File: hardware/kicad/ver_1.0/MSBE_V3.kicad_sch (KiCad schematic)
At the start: 179 parts, among them J1 USB_C_Receptacle_USB2.0_16P, J10 Low-V, J2 USB_C_Receptacle_USB2.0_16P, J3 Touch Pads, J4 Touch Pads, J5 UART, J6 Prog, J7 UART, J8 Prog, J9 High-V, U1 NPM1100-CAAA-R7, U10 MAX98357AEWL_T, U2 NPM1100-CAAA-R7, U3 NRF5340-CLAA-R, U4 NRF5340-CLAA-R, U5 BMA400, U6 BMA400, U7 MPR121QR2, U8 MPR121QR2, U9 MAX98357AEWL_T, Y1 32MHz, Y2 Crystal, Y3 32.768kHz, Y4 32.768kHz, Y5 32MHz

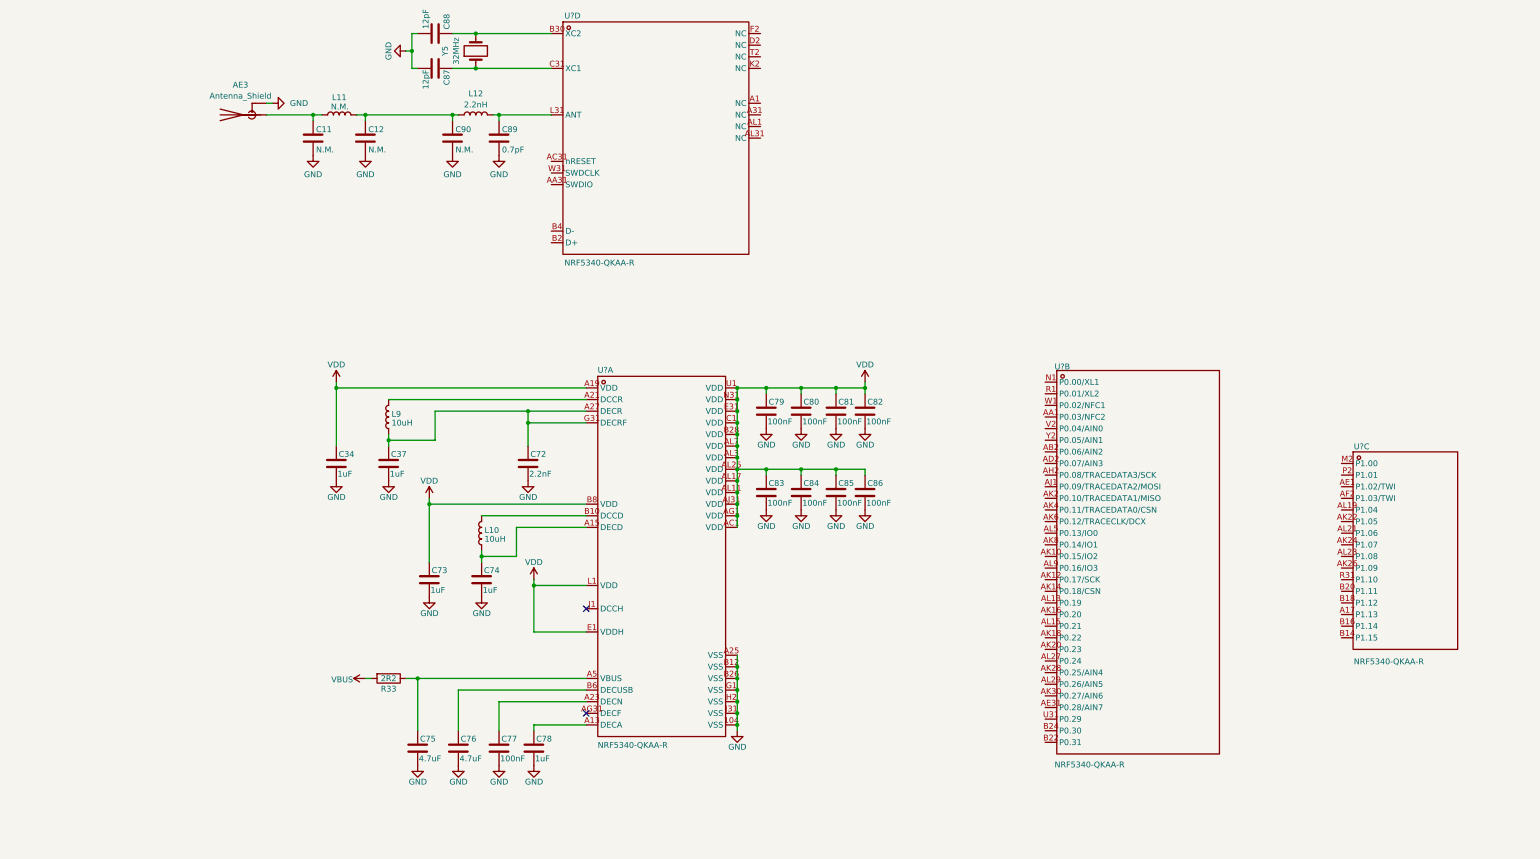
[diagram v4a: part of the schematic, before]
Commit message: updated schematic QFN
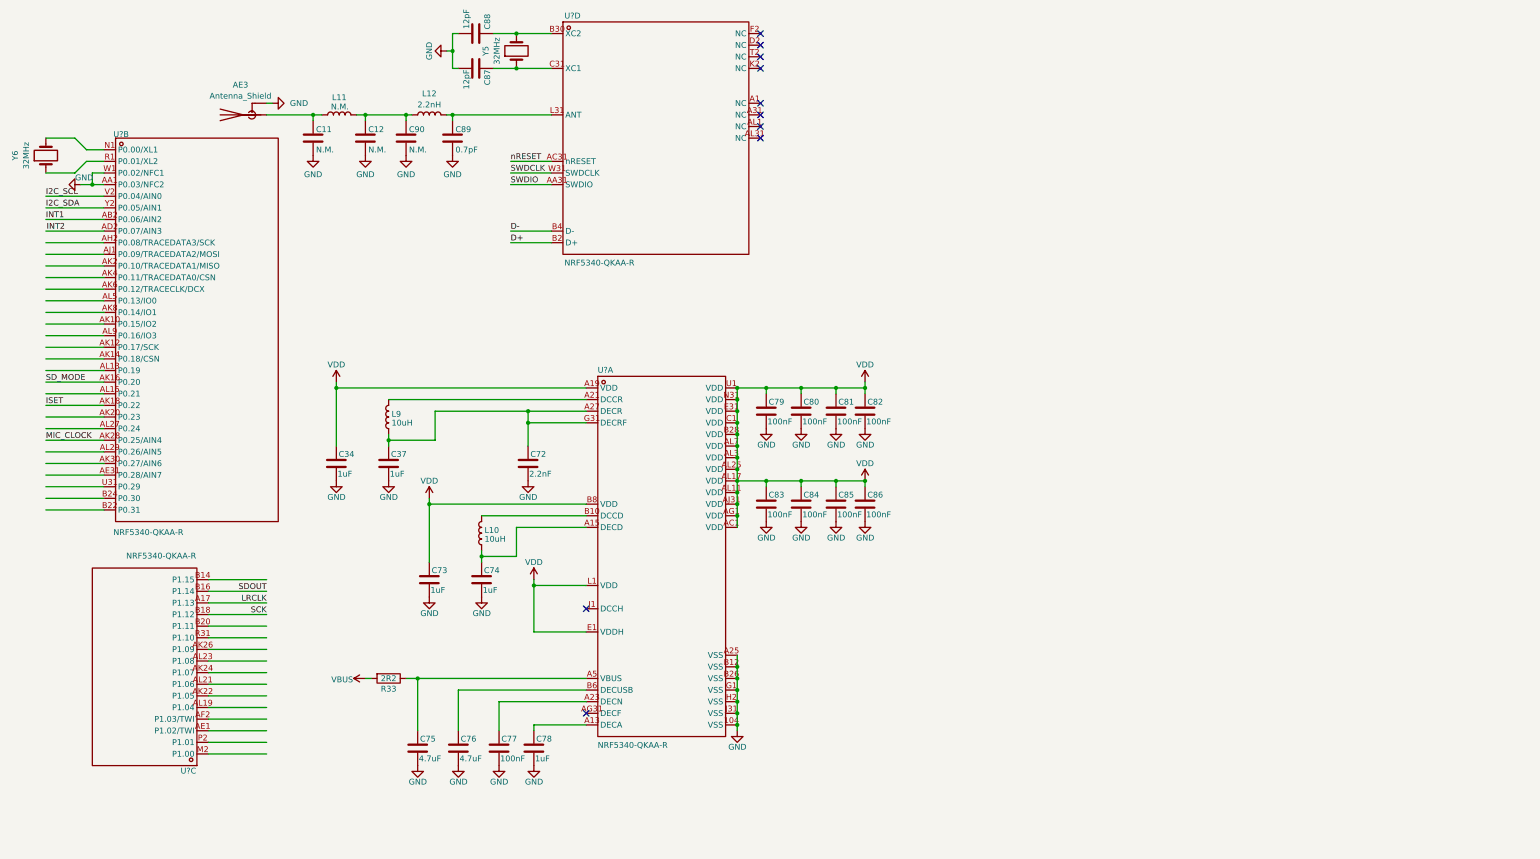
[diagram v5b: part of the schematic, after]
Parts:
- added Y6: 32MHz, mylib:Crystal_24MHz-ECS-240-12-37B-CKY-TR, symbol Device:Crystal
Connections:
- net AVSS: now also U?.AA1 (P0.03/NFC2), U?.W1 (P0.02/NFC1)
- net D+: now also U?.B2 (D+)
- net D-: now also U?.B4 (D-)
- net I2C_SCL: now also U?.V2 (P0.04/AIN0)
- net I2C_SDA: now also U?.Y2 (P0.05/AIN1)
- net INT1: now also U?.AB2 (P0.06/AIN2)
- net INT2: now also U?.AD2 (P0.07/AIN3)
- net ISET: now also U?.AK18 (P0.22)
- net LRCLK: now also U?.A17 (P1.13)
- net MIC_CLOCK: now also U?.AK28 (P0.25/AIN4)
- net SCK: now also U?.B18 (P1.12)
- net SDOUT: now also U?.B16 (P1.14)
- net SD_MODE: now also U?.AK16 (P0.20)
- net SWDCLK: now also U?.W31 (SWDCLK)
- net SWDIO: now also U?.AA31 (SWDIO)
- net nRESET: now also U?.AC31 (nRESET)
- net at U?.N1 (P0.00/XL1): now also Y6.2
- net at U?.R1 (P0.01/XL2): now also Y6.1
- no-connect marks 26 -> 34
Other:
- moved on the sheet: C83, C84, C85, C86, C87, C88, C89, C90, L12, U?B, U?C, Y5

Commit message: update
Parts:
- removed AE1: Antenna_Shield, RF_Antenna:Texas_SWRA117D_2.4GHz_Left, symbol Device:Antenna_Shield
- removed C13, C14: 12pF, Capacitor_SMD:C_0603_1608Metric, symbol Device:C
- removed C15, C17, C21, C22, C29, C30, C31, C32, C45: 1.0uF, Capacitor_SMD:C_0603_1608Metric, symbol Device:C
- removed C16, C18, C19, C20, C25, C26, C27, C28: 100nF, Capacitor_SMD:C_0603_1608Metric, symbol Device:C
- removed C23, C24: 2.2nF, Capacitor_SMD:C_0603_1608Metric, symbol Device:C
- removed C33, C35, C36, C40: 4.7uF, Capacitor_SMD:C_0603_1608Metric, symbol Device:C
- removed C38, C42: N.C., Capacitor_SMD:C_0603_1608Metric, symbol Device:C
- removed C39: 0.7pF, Capacitor_SMD:C_0603_1608Metric, symbol Device:C
- removed C53, C54: 0.1uF, Capacitor_SMD:C_0603_1608Metric, symbol Device:C
- removed L3, L4, L5: 10uH, Inductor_SMD:L_0603_1608Metric, symbol Device:L
- removed R13, R14, R15, R16: 4.7k, Resistor_SMD:R_0603_1608Metric, symbol Device:R
- removed R17, R18: 2R2, Resistor_SMD:R_0603_1608Metric, symbol Device:R
- removed U3, U4: NRF5340-CLAA-R, mylib:NRF5340-CLAA-R, symbol mySch_lib:NRF5340-CLAA-R
- removed Y1: 32MHz, mylib:Crystal_24MHz-ECS-240-12-37B-CKY-TR, symbol Device:Crystal
- removed Y2: Crystal, mylib:Crystal_24MHz-ECS-240-12-37B-CKY-TR, symbol Device:Crystal
- added C57, C59: 4.7uF, Capacitor_SMD:C_0603_1608Metric, symbol Device:C
- added C58, C60, C63: 1uF, Capacitor_SMD:C_0603_1608Metric, symbol Device:C
- added C61, C68, C69, C70, C71, C72, C73, C74, C75: 100nF, Capacitor_SMD:C_0603_1608Metric, symbol Device:C
- added C62: 2.2nF, Capacitor_SMD:C_0603_1608Metric, symbol Device:C
- added J9: Low-V-TH, Connector_PinHeader_2.54mm:PinHeader_1x05_P2.54mm_Vertical, symbol Connector:Conn_01x05_Pin
- added L9: 10uH, Inductor_SMD:L_0603_1608Metric, symbol Device:L
- added R10, R29, R30, R9: 4k7, Resistor_SMD:R_0603_1608Metric, symbol Device:R
- added R26: 2R2, Resistor_SMD:R_0603_1608Metric, symbol Device:R
- added U9: NRF5340-QKAA-R, myLib:NRF5340, symbol 1_MSBE_V3-altium-import:root_0_NRF5340-QKAA-R_
- BT1, BT2: footprint mylib:Pad_3Pin_1.5x0.8mm -> myLib:Pad_3Pin_1.5x0.8mm
- C41, C44: value 100nF -> N.M.
- C43: value 0.7pF -> N.M.
- C46: value 1.0uF -> 0.7pF
- C47, C48: value 100nF -> 12pF
- C55, C56: value 100nF -> 1uF
- J10: renamed from J8; footprint mylib:Pad_prog_4Pad -> myLib:Pad_prog_4Pad
- J11: renamed from J7; footprint mylib:Pad_3Pin_1.5x0.8mm -> myLib:Pad_3Pin_1.5x0.8mm
- J2: renamed from J3; footprint mylib:Pad_3Pin_1.5x0.8mm -> myLib:Pad_3Pin_1.5x0.8mm
- J3: renamed from J5; footprint mylib:Pad_3Pin_1.5x0.8mm -> myLib:Pad_3Pin_1.5x0.8mm
- J4: renamed from J6; footprint mylib:Pad_prog_4Pad -> myLib:Pad_prog_4Pad
- J5: renamed from J4; footprint mylib:Pad_3Pin_1.5x0.8mm -> myLib:Pad_3Pin_1.5x0.8mm
- J6: renamed from J9; footprint mylib:Pad_prog_4Pad -> myLib:Pad_prog_4Pad
- J8: renamed from J10; footprint mylib:Pad_prog_4Pad -> myLib:Pad_prog_4Pad
- L6: value 10uH -> N.M.
- L8: value 2.2nH -> 10uH
- LS1: footprint mylib:MIC_SPH18R1LM4H_KNO -> myLib:MIC_SPH18R1LM4H_KNO
- LS2: renamed from LS3; footprint mylib:Pad_2Pin_1.5x0.8mm -> myLib:Pad_2Pin_1.5x0.8mm
- LS3: renamed from LS4; footprint mylib:Pad_2Pin_1.5x0.8mm -> myLib:Pad_2Pin_1.5x0.8mm
- LS4: renamed from LS5; footprint mylib:Pad_2Pin_1.5x0.8mm -> myLib:Pad_2Pin_1.5x0.8mm
- LS5: renamed from LS6; footprint mylib:Pad_2Pin_1.5x0.8mm -> myLib:Pad_2Pin_1.5x0.8mm
- LS6: renamed from LS2; footprint mylib:MIC_SPH18R1LM4H_KNO -> myLib:MIC_SPH18R1LM4H_KNO
- U1: renamed from U5; footprint mylib:QFN_BMA400_BOS -> myLib:QFN_BMA400_BOS
- U10: renamed from U2; footprint mylib:NPM1100-CAAA-BGA25C40P5X5_207X207X52N -> myLib:NPM1100-CAAA-BGA25C40P5X5_207X207X52N
- U2: renamed from U7; footprint mylib:MPR121 -> myLib:MPR121
- U3: renamed from U?; footprint AQFN-94_L7.0-W7.0-P0.40_NRF5340-QKAA-R -> myLib:NRF5340
- U4: renamed from U1; footprint mylib:NPM1100-CAAA-BGA25C40P5X5_207X207X52N -> myLib:NPM1100-CAAA-BGA25C40P5X5_207X207X52N
- U5: renamed from U9; footprint mylib:MAX98357A_BGA9N40P3X3_134X143X69N -> myLib:MAX98357A_BGA9N40P3X3_134X143X69N
- U6: renamed from U10; footprint mylib:MAX98357A_BGA9N40P3X3_134X143X69N -> myLib:MAX98357A_BGA9N40P3X3_134X143X69N
- U7: renamed from U8; footprint mylib:MPR121 -> myLib:MPR121
- U8: renamed from U6; footprint mylib:QFN_BMA400_BOS -> myLib:QFN_BMA400_BOS
- Y1: renamed from Y5; footprint mylib:Crystal_24MHz-ECS-240-12-37B-CKY-TR -> myLib:ECS-160-10-37-JTN-TR_ECS
- Y2: renamed from Y6; value 32MHz -> 32.768kHz; footprint mylib:Crystal_24MHz-ECS-240-12-37B-CKY-TR -> myLib:Crystal_24MHz-ECS-240-12-37B-CKY-TR
- Y3: value 32.768kHz -> 32MHz; footprint mylib:Crystal_24MHz-ECS-240-12-37B-CKY-TR -> myLib:ECS-160-10-37-JTN-TR_ECS
- Y4: footprint mylib:Crystal_24MHz-ECS-240-12-37B-CKY-TR -> myLib:Crystal_24MHz-ECS-240-12-37B-CKY-TR
- renumbered AE3 to AE1, C49 to C1, C50 to C10, C57 to C11, C34 to C12, C37 to C13, C75 to C14, C73 to C15, C76 to C16, C74 to C17, C77 to C18, C72 to C19, C59 to C2, C78 to C20, C1 to C21, C63 to C22, C69 to C23, C64 to C24, C70 to C25, C3 to C26, C5 to C27, C7 to C28, C65 to C29, C90 to C3, C79 to C30, C83 to C31, C71 to C32, C80 to C33, C84 to C34, C81 to C35, C85 to C36, C82 to C37, C86 to C38, C60 to C39, C12 to C4, C51 to C40, C61 to C42, C67 to C45, C66 to C49, C11 to C5, C62 to C50, C68 to C51, C10 to C53, C58 to C54, C89 to C6, C2 to C64, C4 to C65, C6 to C66, C8 to C67, C88 to C7, C87 to C8, J2 to J7, L11 to L1, L2 to L10, L12 to L2, L9 to L3, L10 to L4, L1 to L5, R19 to R1, R2 to R11, R1 to R12, R20 to R13, R21 to R14, R28 to R15, R23 to R16, R30 to R17, R25 to R18, R26 to R19, R9 to R2, R11 to R20, R12 to R21, R29 to R23, R31 to R25, R7 to R27, R8 to R28, R10 to R3, R4 to R31, R3 to R32, R33 to R4, R27 to R7, R32 to R8
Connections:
- net AVSS: now also C41.2, C44.2, C47.2, C48.2, C55.2, C56.2, C57.2, C58.2, C59.2, C60.2, C61.2, C62.2, C63.2, C68.2, C69.2, C70.2, C71.2, C72.2, C73.2, C74.2, C75.2, U9.104 (VSS), U9.A25 (VSS), U9.AA1 (P0.03/NFC2), U9.B12 (VSS), U9.B26 (VSS), U9.G1 (VSS), U9.H2 (VSS), U9.J31 (VSS), U9.W1 (P0.02/NFC1); no longer C41.1, C44.1, C47.1, C48.1, C55.1, C56.1
- net B1: now also J9.5 (Pin_5)
- net B2: now also J9.4 (Pin_4)
- net B3: now also J9.3 (Pin_3)
- net B4: now also J9.2 (Pin_2)
- net B5: now also J9.1 (Pin_1)
- net D+: now also U9.B2 (D+)
- net D-: now also U9.B4 (D-)
- net I2C_SCL: now also R29.1, R9.1, U9.V2 (P0.04/AIN0)
- net I2C_SDA: now also R10.1, R30.1, U9.Y2 (P0.05/AIN1)
- net INT1: now also U9.AB2 (P0.06/AIN2)
- net INT2: now also U9.AD2 (P0.07/AIN3)
- net ISET: now also U9.AK18 (P0.22)
- net LRCLK: now also U9.A17 (P1.13)
- net MIC_CLOCK: now also U3.AL29 (P0.26/AIN5), U9.AL29 (P0.26/AIN5); no longer U3.AK28 (P0.25/AIN4)
- net MIC_DATA: now also U3.AK28 (P0.25/AIN4), U9.AK28 (P0.25/AIN4)
- net SCK: now also U9.B18 (P1.12)
- net SDOUT: now also U9.B16 (P1.14)
- net SD_MODE: now also U9.AK16 (P0.20)
- net SWDCLK: now also U9.W31 (SWDCLK)
- net SWDIO: now also U9.AA31 (SWDIO)
- net VBUS: now also R26.2
- net VDD: now also C55.1, C58.1, C68.1, C69.1, C70.1, C71.1, C72.1, C73.1, C74.1, C75.1, R10.2, R29.2, R30.2, R9.2, U9.A19 (VDD), U9.AC1 (VDD), U9.AG1 (VDD), U9.AJ31 (VDD), U9.AL11 (VDD), U9.AL17 (VDD), U9.AL25 (VDD), U9.AL3 (VDD), U9.AL7 (VDD), U9.B28 (VDD), U9.B8 (VDD), U9.C1 (VDD), U9.E1 (VDDH), U9.E31 (VDD), U9.L1 (VDD), U9.N31 (VDD), U9.U1 (VDD); no longer C46.1
- net nRESET: now also U9.AC31 (nRESET)
- net at L8.1: now also C56.1, C62.1, U9.A27 (DECR), U9.G31 (DECRF)
- net at L7.2: now also C46.1, U9.L31 (ANT)
- net at L7.1: now also C41.1, C43.1, L6.2; no longer AE2.1 (A)
- net at L8.2: now also U9.A21 (DCCR); no longer C43.1
- net at L6.1: now also AE2.1 (A), C44.1
- net X1: no longer names the net of Y4.2
- net X1: now also U9.N1 (P0.00/XL1); no longer Y3.2
- net X2: no longer names the net of Y4.1
- net X2: now also U9.R1 (P0.01/XL2); no longer Y3.1
- new net: C63.1, U9.A13 (DECA)
- new net: C60.1, L9.1, U9.A15 (DECD)
- new net: C61.1, U9.A23 (DECN)
- new net: C57.1, R26.1, U9.A5 (VBUS)
- new net: L9.2, U9.B10 (DCCD)
- new net: C59.1, U9.B6 (DECUSB)
- new net: C47.1, U9.B30 (XC2), Y3.2
- new net: C48.1, U9.C31 (XC1), Y3.1
- no-connect marks 34 -> 44
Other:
- note removed: "ISET LOW = 100mA USB limit ISET HIGH = 500mA USB limit"
- moved on the sheet: AE1, BT1, BT2, C1, C10, C11, C12, C13, C14, C15, C16, C17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
